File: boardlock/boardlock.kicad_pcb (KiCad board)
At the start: 2 copper layers, 101 x 76.2 mm, 130 parts, among them J1 Conn_01x02, J2 Conn_01x02, J3 Conn_01x02, J4 Conn_01x02, J5 5033981892, J6 USB_C_Receptacle_USB2.0, Q1 BSS84PWH6327XTSA1, Q2 MMBT4401, Q3 BSS84PWH6327XTSA1, Q4 DTC124X, Q5 DTC124X, Q6 DTC124X, Q7 DTC124X, SW1 SW_Push, SW2 SW_Push, SW3 SW_Push, SW4 SW_Push, SW5 SW_Push, U1 ESP32-S3-WROOM-1, U2 LSM6DSO32, U3 SAM-M8Q, U4 BQ24075RGT, U5 BQ27441DRZR-G1A, U6 TPS630701RNMR, U7 MCP1661, U8 MAX98357AETE+T, U9 TPD2E2U06

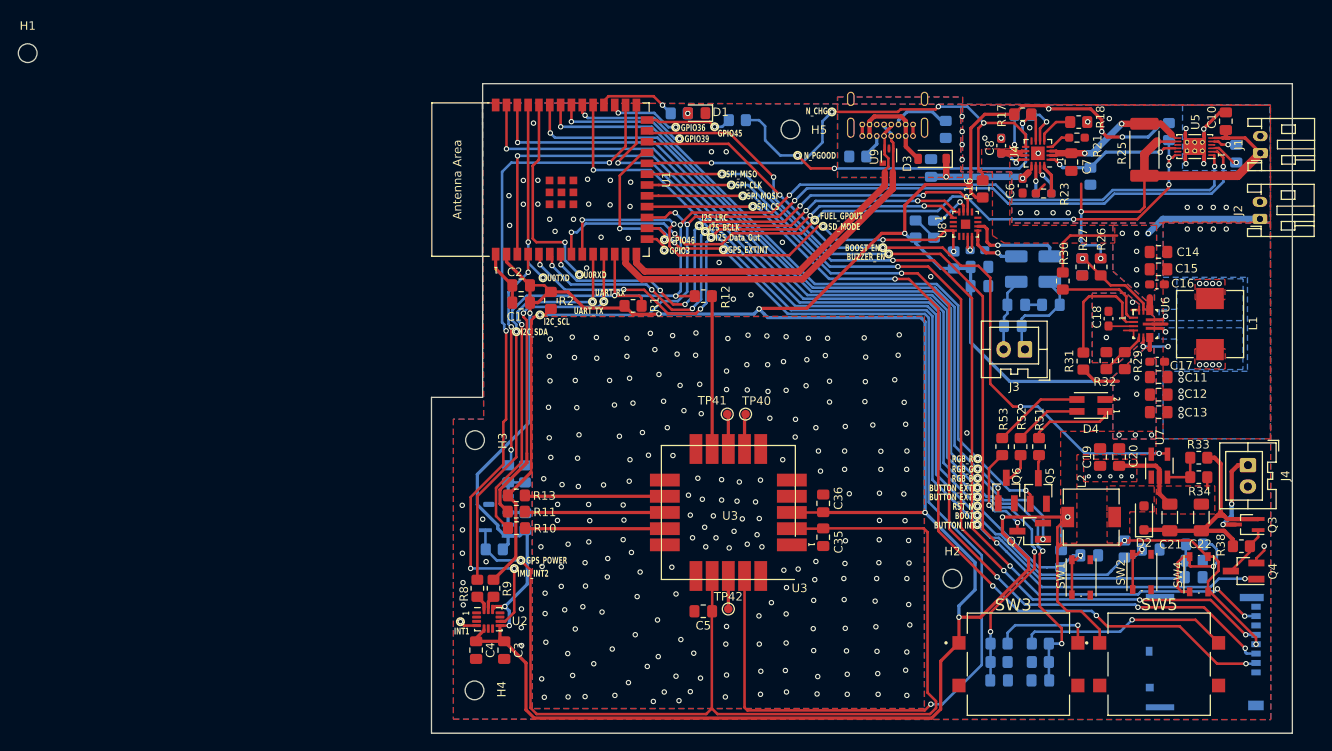
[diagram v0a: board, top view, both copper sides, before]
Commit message: Nick adding Stitch and DRC fixes
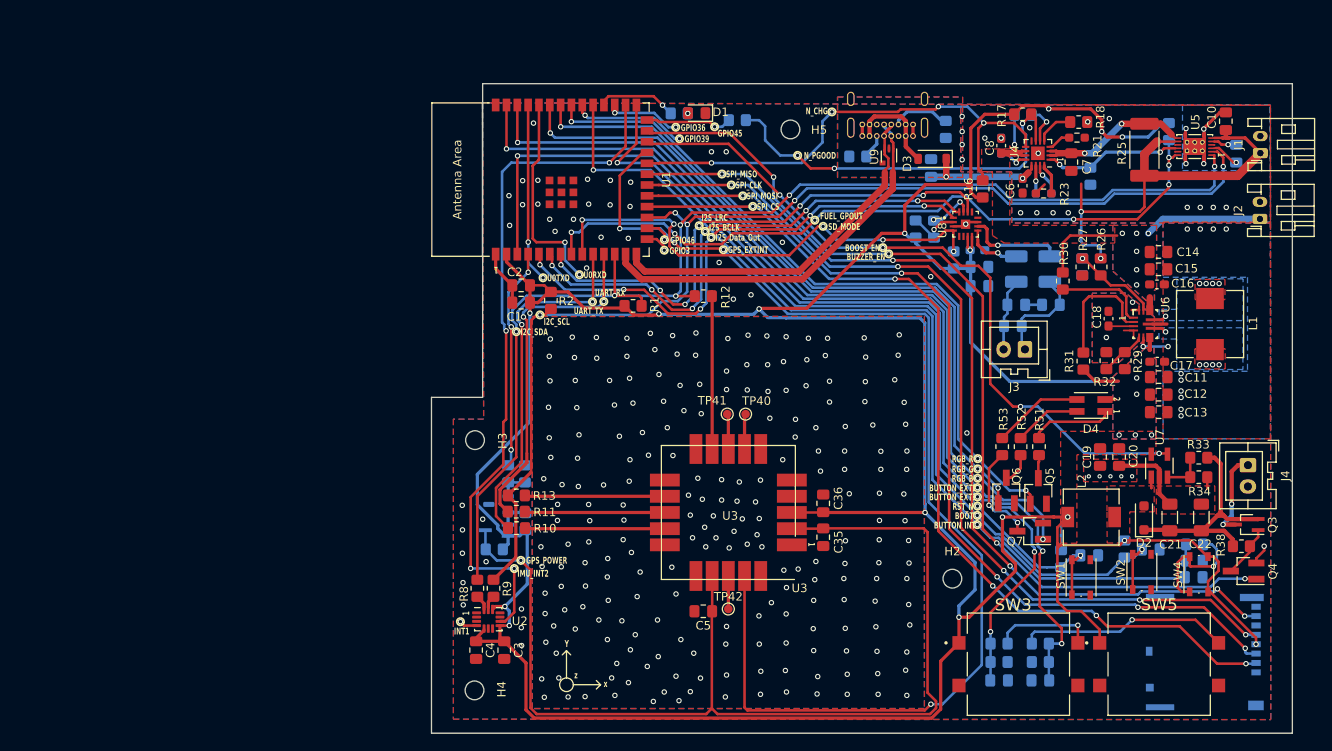
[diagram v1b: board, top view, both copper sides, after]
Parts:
- removed H1: MountingHole, MountingHole:MountingHole_2.2mm_M2
- added G***: LOGO, LOGO, B.Cu at (141.0, 98.8)
- added G***: LOGO, LOGO, B.Cu at (124.6, 132.0)
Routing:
- net GAIN_SLOT: track 2.99 -> 6.58 mm, vias 0 -> 1
- net GND: track 53.0 -> 56.2 mm, vias 293 -> 300
- net Net-(D2-A): track 0.00 -> 1.28 mm
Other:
- board text added: "TEAM 13 10-12-2023, Version 1.0 Zecong Liang Nicholas Williams Jamie Lam David Reed"
- board text added: "Y"
- board text added: "x"
- board text added: "z"
- board text removed: "Testpoints to Check"
- board text removed: "Testpoints to Delete"

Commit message: button and power fixes
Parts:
- SW3, SW5: value SW_Push -> TL3300DF160Q
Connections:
- SW3 pad 2: Net-(R45-Pad1) -> unconnected-(SW3-Pad2)
- SW3 pad 3: (no net) -> Net-(R45-Pad1)
- SW3 pad 4: (no net) -> unconnected-(SW3-Pad4)
- SW5 pad 2: Net-(R49-Pad1) -> unconnected-(SW5-Pad2)
- SW5 pad 3: (no net) -> Net-(R49-Pad1)
- SW5 pad 4: (no net) -> unconnected-(SW5-Pad4)
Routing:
- net Net-(R49-Pad1): track 24.8 -> 10.1 mm
- net Net-(R45-Pad1): track 12.0 -> 7.82 mm
- net BATTERY_IN: track 50.5 -> 47.2 mm
- net GND: track 56.2 -> 53.4 mm, vias 300 -> 303
- net +3V3: track 441.9 -> 439.8 mm, vias 21 -> 20
- net M_GPS_EXTINT: track 140.1 -> 139.0 mm
- net +BATT: vias 2 -> 0

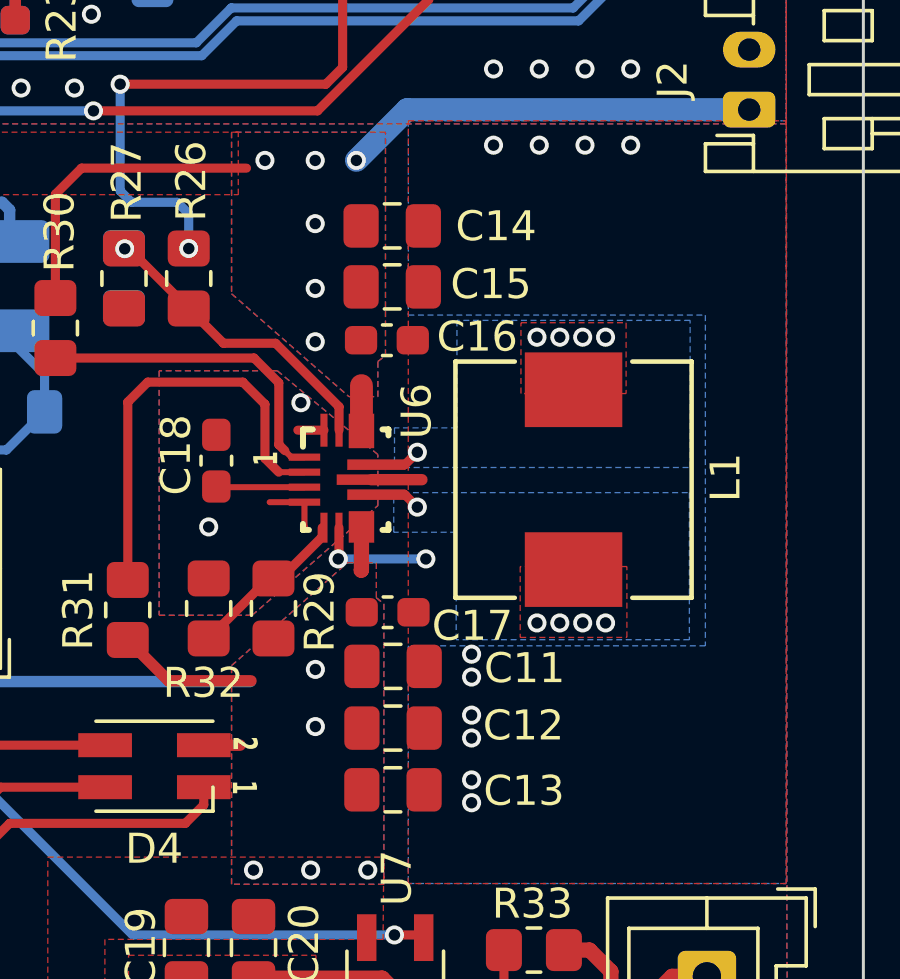
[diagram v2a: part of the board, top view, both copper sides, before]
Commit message: added vias to not get flamed
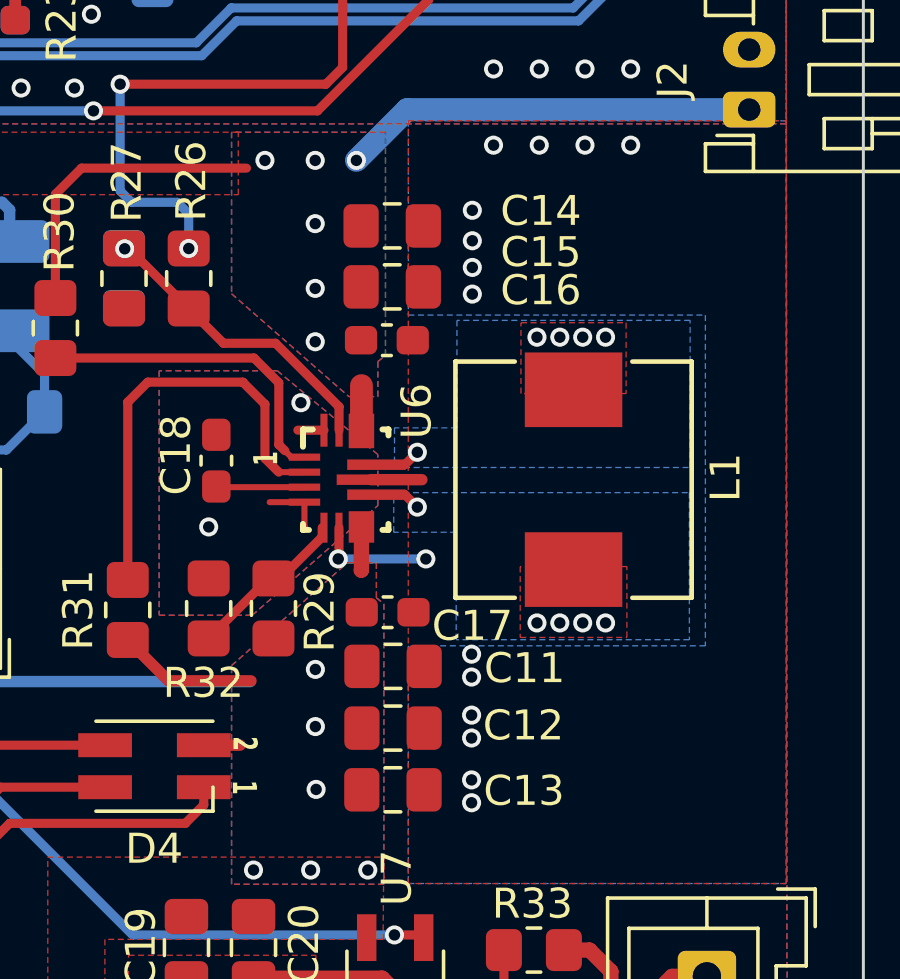
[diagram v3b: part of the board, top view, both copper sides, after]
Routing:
- net GND: vias 303 -> 307
- net +3V3: vias 20 -> 21
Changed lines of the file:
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@@
     (clearance 0.254)
     (attr smd)
-    (fp_text reference "C14" (at 3.4631 0.0136) (layer "F.SilkS")
+    (fp_text reference "C14" (at 4.9561 -0.496) (layer "F.SilkS")
         (effects (font (size 1 1) (thickness 0.15)))
     )
@@
     (clearance 0.254)
     (attr smd)
-    (fp_text reference "C16" (at 3.0109 -0.1164 180) (layer "F.SilkS")
+    (fp_text reference "C16" (at 5.1339 -1.6644 180) (layer "F.SilkS")
         (effects (font (size 1 1) (thickness 0.15)))
     )
@@
     (clearance 0.254)
     (attr smd)
-    (fp_text reference "C15" (at 3.2931 -0.0884) (layer "F.SilkS")
+    (fp_text reference "C15" (at 4.9561 -1.1564) (layer "F.SilkS")
         (effects (font (size 1 1) (thickness 0.15)))
     )
@@
   (via (at 133.84 91.49) (size 0.635) (drill 0.381) (layers "F.Cu" "B.Cu") (net 1))
   (via (at 189.8954 100.9142) (size 0.635) (drill 0.381) (layers "F.Cu" "B.Cu") (free) (net 1))
+  (via (at 189.92 103.009) (size 0.635) (drill 0.381) (layers "F.Cu" "B.Cu") (free) (net 1))
   (via (at 188.468 118.0752) (size 0.635) (drill 0.381) (layers "F.Cu" "B.Cu") (net 1))
   (via (at 165.07 114.79) (size 0.635) (drill 0.381) (layers "F.Cu" "B.Cu") (net 1))
@@
   (via (at 122.39 123.46) (size 0.635) (drill 0.381) (layers "F.Cu" "B.Cu") (free) (net 103))
   (via (at 123.19 136.43) (size 0.635) (drill 0.381) (layers "F.Cu" "B.Cu") (free) (net 103))
+  (via (at 195.127 85.61) (size 0.635) (drill 0.381) (layers "F.Cu" "B.Cu") (free) (net 103))
   (via (at 126.55 96.69) (size 0.635) (drill 0.381) (layers "F.Cu" "B.Cu") (free) (net 103))
   (via (at 130.09 94.35) (size 0.635) (drill 0.381) (layers "F.Cu" "B.Cu") (free) (net 103))
   (via (at 128.15 75.82) (size 0.635) (drill 0.381) (layers "F.Cu" "B.Cu") (free) (net 103))
+  (via (at 195.127 86.499) (size 0.635) (drill 0.381) (layers "F.Cu" "B.Cu") (free) (net 103))
   (via (at 187.06 74.84) (size 0.635) (drill 0.381) (layers "F.Cu" "B.Cu") (free) (net 103))
   (via (at 117.72 126.11) (size 0.635) (drill 0.381) (layers "F.Cu" "B.Cu") (free) (net 103))
@@
   (via (at 157.93 94.3) (size 0.635) (drill 0.381) (layers "F.Cu" "B.Cu") (free) (net 103))
   (via (at 195.834 78.994) (size 0.635) (drill 0.381) (layers "F.Cu" "B.Cu") (free) (net 103))
+  (via (at 195.127 84.721) (size 0.635) (drill 0.381) (layers "F.Cu" "B.Cu") (free) (net 103))
   (via (at 178.8522 75.2081) (size 0.635) (drill 0.381) (layers "F.Cu" "B.Cu") (net 103))
   (via (at 162.91 109.73) (size 0.635) (drill 0.381) (layers "F.Cu" "B.Cu") (free) (net 103))
   (via (at 113.57 120.56) (size 0.635) (drill 0.381) (layers "F.Cu" "B.Cu") (free) (net 103))
+  (via (at 195.127 83.705) (size 0.635) (drill 0.381) (layers "F.Cu" "B.Cu") (free) (net 103))
   (via (at 122.48 111.52) (size 0.635) (drill 0.381) (layers "F.Cu" "B.Cu") (free) (net 103))
   (via (at 152.56 107.58) (size 0.635) (drill 0.381) (layers "F.Cu" "B.Cu") (free) (net 103))

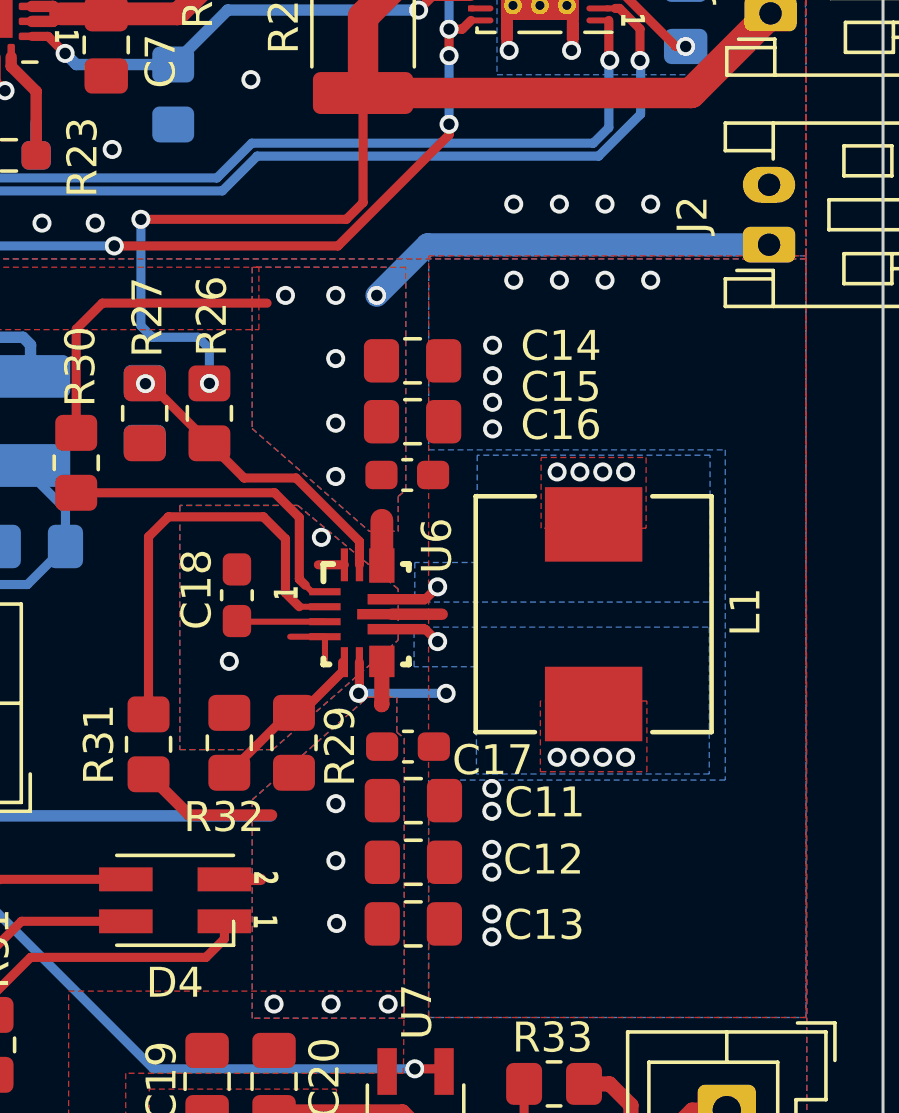
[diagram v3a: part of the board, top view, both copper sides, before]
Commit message: zecong adds a single via
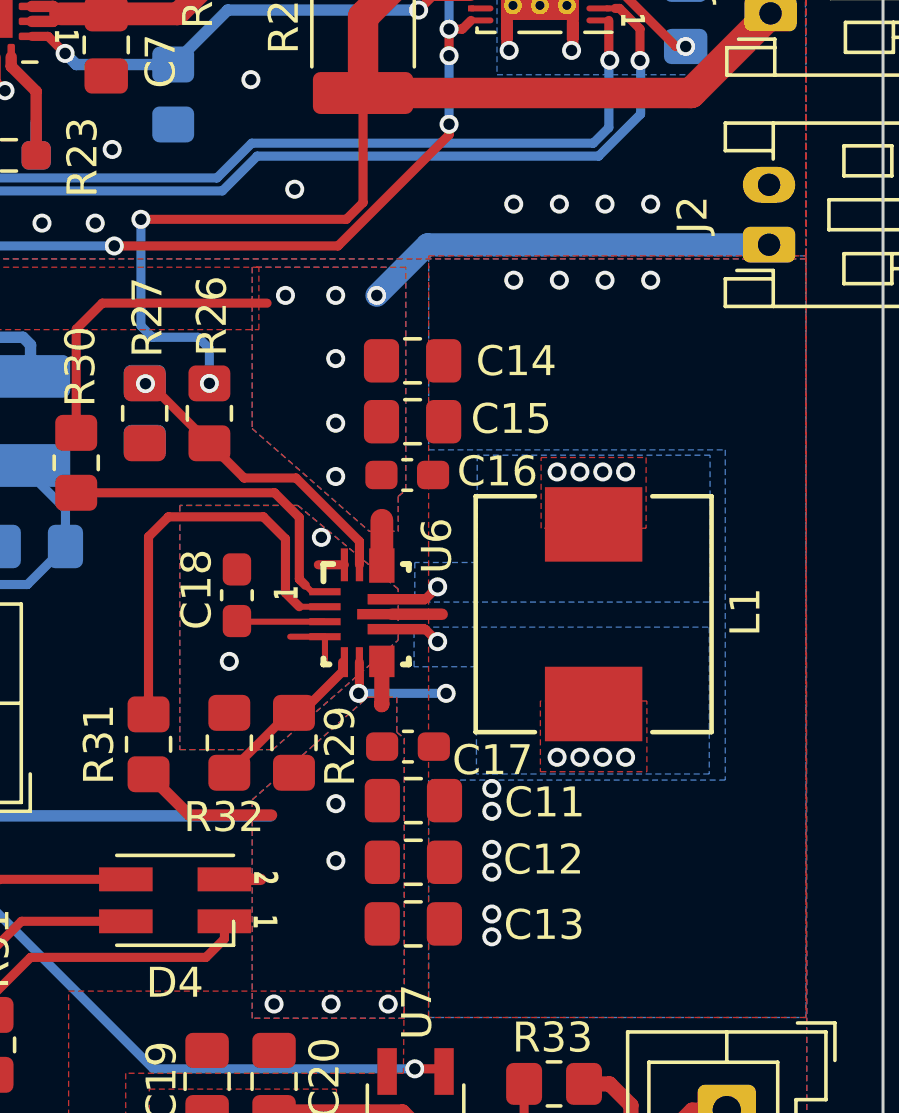
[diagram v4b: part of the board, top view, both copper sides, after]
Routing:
- net GND: vias 307 -> 304
- net +3V3: vias 21 -> 20
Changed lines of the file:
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@@
     (clearance 0.254)
     (attr smd)
-    (fp_text reference "C14" (at 4.9561 -0.496) (layer "F.SilkS")
+    (fp_text reference "C14" (at 3.4631 0.0136) (layer "F.SilkS")
         (effects (font (size 1 1) (thickness 0.15)))
     )
@@
     (clearance 0.254)
     (attr smd)
-    (fp_text reference "C16" (at 5.1339 -1.6644 180) (layer "F.SilkS")
+    (fp_text reference "C16" (at 3.0109 -0.1164 180) (layer "F.SilkS")
         (effects (font (size 1 1) (thickness 0.15)))
     )
@@
     (clearance 0.254)
     (attr smd)
-    (fp_text reference "C15" (at 4.9561 -1.1564) (layer "F.SilkS")
+    (fp_text reference "C15" (at 3.2931 -0.0884) (layer "F.SilkS")
         (effects (font (size 1 1) (thickness 0.15)))
     )
@@
   (via (at 133.84 91.49) (size 0.635) (drill 0.381) (layers "F.Cu" "B.Cu") (net 1))
   (via (at 189.8954 100.9142) (size 0.635) (drill 0.381) (layers "F.Cu" "B.Cu") (free) (net 1))
-  (via (at 189.92 103.009) (size 0.635) (drill 0.381) (layers "F.Cu" "B.Cu") (free) (net 1))
   (via (at 188.468 118.0752) (size 0.635) (drill 0.381) (layers "F.Cu" "B.Cu") (net 1))
   (via (at 165.07 114.79) (size 0.635) (drill 0.381) (layers "F.Cu" "B.Cu") (net 1))
@@
   (via (at 122.39 123.46) (size 0.635) (drill 0.381) (layers "F.Cu" "B.Cu") (free) (net 103))
   (via (at 123.19 136.43) (size 0.635) (drill 0.381) (layers "F.Cu" "B.Cu") (free) (net 103))
-  (via (at 195.127 85.61) (size 0.635) (drill 0.381) (layers "F.Cu" "B.Cu") (free) (net 103))
   (via (at 126.55 96.69) (size 0.635) (drill 0.381) (layers "F.Cu" "B.Cu") (free) (net 103))
   (via (at 130.09 94.35) (size 0.635) (drill 0.381) (layers "F.Cu" "B.Cu") (free) (net 103))
   (via (at 128.15 75.82) (size 0.635) (drill 0.381) (layers "F.Cu" "B.Cu") (free) (net 103))
-  (via (at 195.127 86.499) (size 0.635) (drill 0.381) (layers "F.Cu" "B.Cu") (free) (net 103))
   (via (at 187.06 74.84) (size 0.635) (drill 0.381) (layers "F.Cu" "B.Cu") (free) (net 103))
   (via (at 117.72 126.11) (size 0.635) (drill 0.381) (layers "F.Cu" "B.Cu") (free) (net 103))
@@
   (via (at 157.93 94.3) (size 0.635) (drill 0.381) (layers "F.Cu" "B.Cu") (free) (net 103))
   (via (at 195.834 78.994) (size 0.635) (drill 0.381) (layers "F.Cu" "B.Cu") (free) (net 103))
-  (via (at 195.127 84.721) (size 0.635) (drill 0.381) (layers "F.Cu" "B.Cu") (free) (net 103))
   (via (at 178.8522 75.2081) (size 0.635) (drill 0.381) (layers "F.Cu" "B.Cu") (net 103))
   (via (at 162.91 109.73) (size 0.635) (drill 0.381) (layers "F.Cu" "B.Cu") (free) (net 103))
   (via (at 113.57 120.56) (size 0.635) (drill 0.381) (layers "F.Cu" "B.Cu") (free) (net 103))
-  (via (at 195.127 83.705) (size 0.635) (drill 0.381) (layers "F.Cu" "B.Cu") (free) (net 103))
+  (via (at 188.523 78.498) (size 0.635) (drill 0.381) (layers "F.Cu" "B.Cu") (free) (net 103))
   (via (at 122.48 111.52) (size 0.635) (drill 0.381) (layers "F.Cu" "B.Cu") (free) (net 103))
   (via (at 152.56 107.58) (size 0.635) (drill 0.381) (layers "F.Cu" "B.Cu") (free) (net 103))
